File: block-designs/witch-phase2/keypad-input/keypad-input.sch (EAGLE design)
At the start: 33 parts, among them SW0 SWITCH-MOMENTARY-212MM, SW1 SWITCH-MOMENTARY-212MM, SW2 SWITCH-MOMENTARY-212MM, SW3 SWITCH-MOMENTARY-212MM, SW4 SWITCH-MOMENTARY-212MM, SW5 SWITCH-MOMENTARY-212MM, SW6 SWITCH-MOMENTARY-212MM, SW7 SWITCH-MOMENTARY-212MM, SW8 SWITCH-MOMENTARY-212MM, SW9 SWITCH-MOMENTARY-212MM

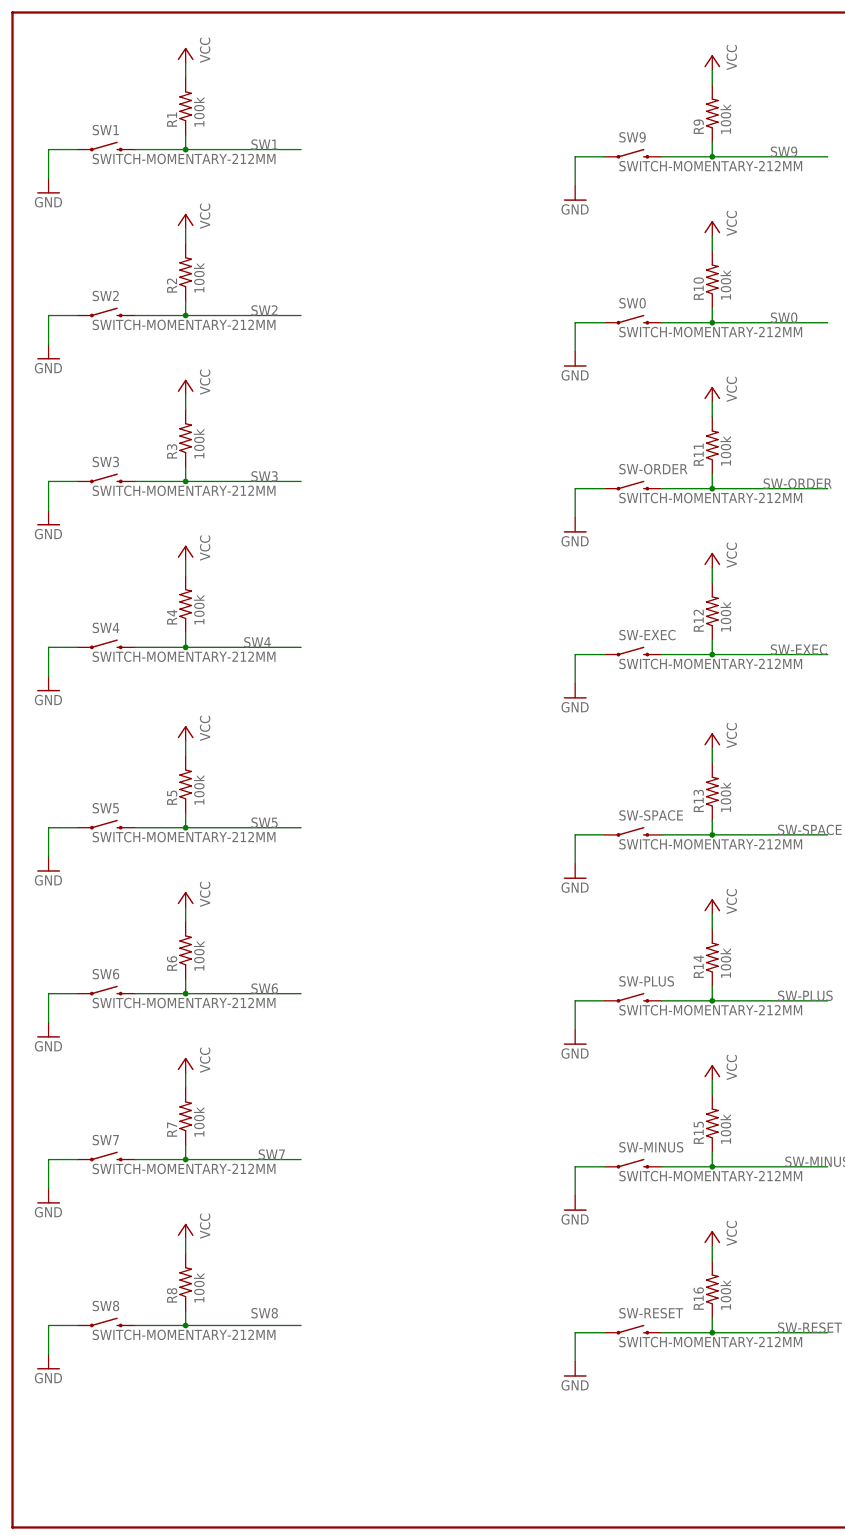
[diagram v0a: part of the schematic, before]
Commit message: change polarity of buttons to active high
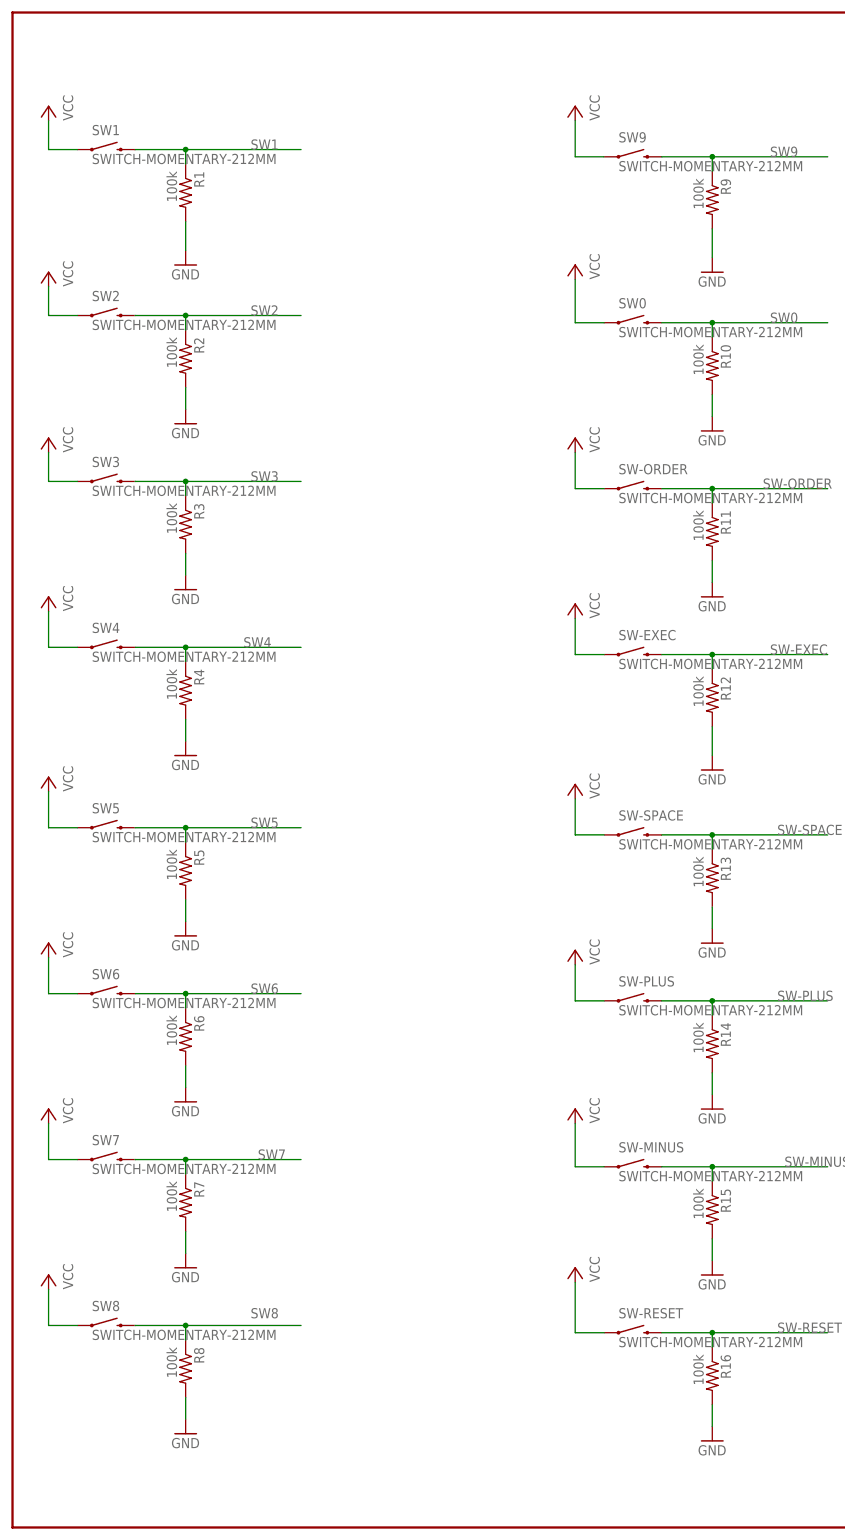
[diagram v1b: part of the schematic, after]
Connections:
- net GND: now also R1.2, R10.2, R11.2, R12.2, R13.2, R14.2, R15.2, R16.2, R2.2, R3.2, R4.2, R5.2, R6.2, R7.2, R8.2, R9.2; no longer SW-EXEC.1, SW-MINUS.1, SW-ORDER.1, SW-PLUS.1, SW-RESET.1, SW-SPACE.1, SW0.1, SW1.1, SW2.1, SW3.1, SW4.1, SW5.1, SW6.1, SW7.1, SW8.1, SW9.1
- net VCC: now also SW-EXEC.1, SW-MINUS.1, SW-ORDER.1, SW-PLUS.1, SW-RESET.1, SW-SPACE.1, SW0.1, SW1.1, SW2.1, SW3.1, SW4.1, SW5.1, SW6.1, SW7.1, SW8.1, SW9.1; no longer R1.2, R10.2, R11.2, R12.2, R13.2, R14.2, R15.2, R16.2, R2.2, R3.2, R4.2, R5.2, R6.2, R7.2, R8.2, R9.2
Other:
- moved on the sheet: R1, R10, R11, R12, R13, R14, R15, R16, R2, R3, R4, R5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
